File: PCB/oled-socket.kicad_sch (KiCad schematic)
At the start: 16 parts, among them IC17 TPS6734IDR, J5 3-2328724-1

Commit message: change OLED voltage converter to compatible (in-stock) part
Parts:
- IC17: value TPS6734IDR -> TPS6734ID; Arrow Part Number TPS6734IDR -> TPS6734ID; Mouser Part Number 595-TPS6734IDR -> 595-TPS6734ID
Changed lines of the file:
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@@
       (effects (font (size 1.27 1.27)))
     )
-    (property "Value" "TPS6734IDR" (at 207.01 103.0279 0)
+    (property "Value" "TPS6734ID" (at 207.01 103.0279 0)
       (effects (font (size 1.27 1.27)))
     )
@@
       (effects (font (size 1.27 1.27)) (justify left) hide)
     )
-    (property "Mouser Part Number" "595-TPS6734IDR" (at 217.17 119.38 0)
+    (property "Mouser Part Number" "595-TPS6734ID" (at 217.17 119.38 0)
       (effects (font (size 1.27 1.27)) (justify left) hide)
     )
@@
       (effects (font (size 1.27 1.27)) (justify left) hide)
     )
-    (property "Arrow Part Number" "TPS6734IDR" (at 217.17 124.46 0)
+    (property "Arrow Part Number" "TPS6734ID" (at 217.17 124.46 0)
       (effects (font (size 1.27 1.27)) (justify left) hide)
     )
@@
     )
     (property "Note" "RM \"R\" SUFFIX FOR CPT. PART" (at 207.01 118.11 0)
-      (effects (font (size 1.27 1.27)))
+      (effects (font (size 1.27 1.27)) hide)
     )
     (pin "1")

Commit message: add pullup/down resistors and fix oro 6p lines with boot1/0
closes #24
closes #21
closes #15
closes #12
closes #6
closes #3
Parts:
- added R10 (x2): 10k, SamacSys_Parts:RESC5025X65N, symbol SamacSys_Parts:RC2010JK-0710KL
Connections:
- net +3V3: now also R10.1
- net CS: now also R10.2
- net GND: now also R10.1
- net ~{RST}: now also R10.2

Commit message: put pulldowns on unused OLED data lines and add a 510k to pin 13
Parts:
- removed R10: 10k, SamacSys_Parts:RESC5025X65N, symbol SamacSys_Parts:RC2010JK-0710KL
- added R10 (x7): 10k, SamacSys_Parts:RESC5025X65N, symbol SamacSys_Parts:RC2010JK-0710KL
- added R13: 510K, RESC1608X55N, symbol SamacSys_Parts:CR0603-JW-514ELF
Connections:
- net GND: now also R10.2, R10.2, R10.2, R10.2, R10.2, R10.2, R10.2, R13.2; no longer J5.24, J5.25, J5.26, J5.27, J5.28, J5.29
- net ~{RST}: now also R10.1
- net at J5.7: now also R13.1
- new net D2: J5.24, R10.1
- new net D3: J5.25, R10.1
- new net D4: J5.26, R10.1
- new net D5: J5.27, R10.1
- new net D6: J5.28, R10.1
- new net D7: J5.29, R10.1
- no-connect marks 6 -> 5
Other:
- note added: "10K"
- moved on the sheet: C20, C21, R10

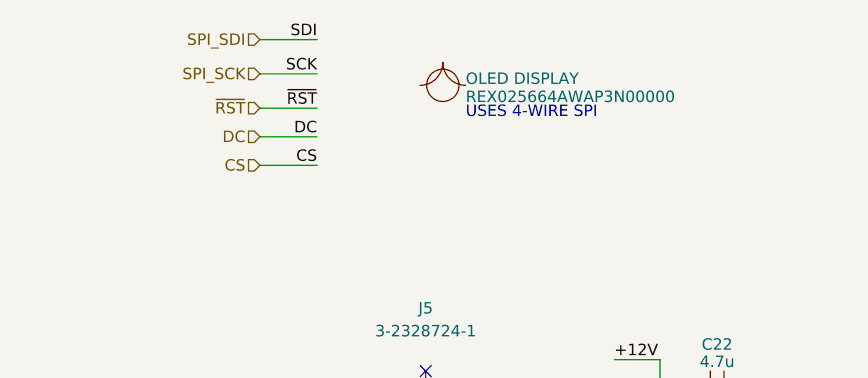
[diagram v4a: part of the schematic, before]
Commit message: add debug pins to signal lines (closes #16)
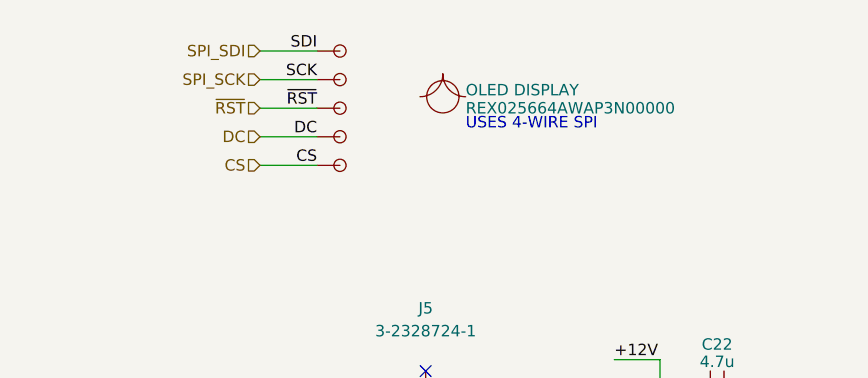
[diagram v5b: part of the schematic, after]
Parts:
- added DBG5 (x5): ~, Oro Footprints:DebugPin, symbol Oro:DebugPin
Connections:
- net CS: now also DBG5.1
- net DC: now also DBG5.1
- net SPI_SCK: now also DBG5.1
- net SPI_SDI: now also DBG5.1
- net ~{RST}: now also DBG5.1
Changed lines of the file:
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@@
     (stroke (width 0) (type default))
   )
-  (wire (pts (xy 67.945 40.64) (xy 74.295 40.64))
+  (wire (pts (xy 67.945 41.91) (xy 74.295 41.91))
     (stroke (width 0) (type default))
   )
@@
     (stroke (width 0) (type default))
   )
-  (wire (pts (xy 67.945 44.45) (xy 74.295 44.45))
+  (wire (pts (xy 67.945 45.085) (xy 74.295 45.085))
     (stroke (width 0) (type default))
   )
@@
     (effects (font (size 1.27 1.27)) (justify left bottom))
   )
-  (text "USES 4-WIRE SPI" (at 90.805 49.53 0)
+  (text "USES 4-WIRE SPI" (at 90.805 50.8 0)
     (effects (font (size 1.27 1.27)) (justify left bottom))
   )
@@
     (effects (font (size 1.27 1.27)) (justify right bottom))
   )
-  (label "SDI" (at 74.295 40.64 180) (fields_autoplaced)
+  (label "SDI" (at 74.295 41.91 180) (fields_autoplaced)
     (effects (font (size 1.27 1.27)) (justify right bottom))
   )
@@
     (effects (font (size 1.27 1.27)) (justify right bottom))
   )
-  (label "SCK" (at 74.295 44.45 180) (fields_autoplaced)
+  (label "SCK" (at 74.295 45.085 180) (fields_autoplaced)
     (effects (font (size 1.27 1.27)) (justify right bottom))
   )
@@
     (effects (font (size 1.27 1.27)) (justify right))
   )
-  (hierarchical_label "SPI_SDI" (shape input) (at 67.945 40.64 180) (fields_autoplaced)
+  (hierarchical_label "SPI_SDI" (shape input) (at 67.945 41.91 180) (fields_autoplaced)
     (effects (font (size 1.27 1.27)) (justify right))
   )
-  (hierarchical_label "SPI_SCK" (shape input) (at 67.945 44.45 180) (fields_autoplaced)
+  (hierarchical_label "SPI_SCK" (shape input) (at 67.945 45.085 180) (fields_autoplaced)
     (effects (font (size 1.27 1.27)) (justify right))
   )
@@
     )
   )
-  (symbol (lib_id "Oro:BOM Part") (at 88.265 45.72 0) (unit 1)
+  (symbol (lib_id "Oro:BOM Part") (at 88.265 46.99 0) (unit 1)
     (in_bom yes) (on_board no) (dnp no)
-    (property "Reference" "B2" (at 90.17 45.0763 0)
-      (effects (font (size 1.27 1.27)) (justify left) hide)
-    )
-    (property "Value" "REX025664AWAP3N00000" (at 90.805 46.99 0)
+    (property "Reference" "B2" (at 90.17 46.3463 0)
+      (effects (font (size 1.27 1.27)) (justify left) hide)
+    )
+    (property "Value" "REX025664AWAP3N00000" (at 90.805 48.26 0)
       (effects (font (size 1.27 1.27)) (justify left))
     )
-    (property "Footprint" "" (at 88.265 45.72 0)
-      (effects (font (size 1.27 1.27)) hide)
-    )
-    (property "Datasheet" "https://www.mouser.de/datasheet/2/271/REX025664AWAP3N00000_V_E_20191218-1888866.pdf" (at 88.265 45.72 0)
-      (effects (font (size 1.27 1.27)) hide)
-    )
-    (property "Sim.Enable" "0" (at 88.265 45.72 0)
-      (effects (font (size 1.27 1.27)) hide)
-    )
-    (property "Manufacturer_Part_Number" "REX025664AWAP3N00000" (at 88.265 45.72 0)
-      (effects (font (size 1.27 1.27)) hide)
-    )
-    (property "Mouser Part Number" "668-REX025664AWAP3N" (at 88.265 45.72 0)
-      (effects (font (size 1.27 1.27)) hide)
-    )
-    (property "Note" "OLED DISPLAY" (at 90.805 45.72 0)
+    (property "Footprint" "" (at 88.265 46.99 0)
+      (effects (font (size 1.27 1.27)) hide)
+    )
+    (property "Datasheet" "https://www.mouser.de/datasheet/2/271/REX025664AWAP3N00000_V_E_20191218-1888866.pdf" (at 88.265 46.99 0)
+      (effects (font (size 1.27 1.27)) hide)
+    )
+    (property "Sim.Enable" "0" (at 88.265 46.99 0)
+      (effects (font (size 1.27 1.27)) hide)
+    )
+    (property "Manufacturer_Part_Number" "REX025664AWAP3N00000" (at 88.265 46.99 0)
+      (effects (font (size 1.27 1.27)) hide)
+    )
+    (property "Mouser Part Number" "668-REX025664AWAP3N" (at 88.265 46.99 0)
+      (effects (font (size 1.27 1.27)) hide)
+    )
+    (property "Note" "OLED DISPLAY" (at 90.805 46.99 0)
       (effects (font (size 1.27 1.27)) (justify left bottom))
     )
@@
     )
   )
+  (symbol (lib_id "Oro:DebugPin") (at 74.295 45.085 0) (unit 1)
+    (in_bom no) (on_board yes) (dnp no)
+    (property "Reference" "DBG5" (at 80.01 45.085 0)
+      (effects (font (size 1.27 1.27)) hide)
+    )
+    (property "Value" "~" (at 74.295 45.085 0)
+      (effects (font (size 1.27 1.27)) hide)
+    )
+    (property "Footprint" "Oro Footprints:DebugPin" (at 75.565 42.545 0)
+      (effects (font (size 1.27 1.27)) hide)
+    )
+    (property "Datasheet" "" (at 74.295 45.085 0)
+      (effects (font (size 1.27 1.27)) hide)
+    )
+    (property "Sim.Enable" "0" (at 88.265 42.545 0)
+      (effects (font (size 1.27 1.27)) hide)
+    )
+    (pin "1")
+    (instances
+      (project "OroLink"
+        (path "/e89dcd22-1250-4a5b-b778-1c95a0dd623d/f955395e-bf1a-4ef3-9cfe-ec9d49f66988"
+          (reference "DBG5") (unit 1)
+        )
+        (path "/e89dcd22-1250-4a5b-b778-1c95a0dd623d/1b3eede1-74b0-4c0b-b4f1-7ec1bfc1f54f"
+          (reference "DBG13") (unit 1)
+        )
+      )
+    )
+  )
   (symbol (lib_id "SamacSys_Parts:CR0603-JW-514ELF") (at 50.165 97.79 270) (unit 1)
     (in_bom yes) (on_board yes) (dnp no) (fields_autoplaced)
@@
     )
   )
+  (symbol (lib_id "Oro:DebugPin") (at 74.295 41.91 0) (unit 1)
+    (in_bom no) (on_board yes) (dnp no)
+    (property "Reference" "DBG5" (at 80.01 41.91 0)
+      (effects (font (size 1.27 1.27)) hide)
+    )
+    (property "Value" "~" (at 74.295 41.91 0)
+      (effects (font (size 1.27 1.27)) hide)
+    )
+    (property "Footprint" "Oro Footprints:DebugPin" (at 75.565 39.37 0)
+      (effects (font (size 1.27 1.27)) hide)
+    )
+    (property "Datasheet" "" (at 74.295 41.91 0)
+      (effects (font (size 1.27 1.27)) hide)
+    )
+    (property "Sim.Enable" "0" (at 88.265 39.37 0)
+      (effects (font (size 1.27 1.27)) hide)
+    )
+    (pin "1")
+    (instances
+      (project "OroLink"
+        (path "/e89dcd22-1250-4a5b-b778-1c95a0dd623d/f955395e-bf1a-4ef3-9cfe-ec9d49f66988"
+          (reference "DBG5") (unit 1)
+        )
+        (path "/e89dcd22-1250-4a5b-b778-1c95a0dd623d/1b3eede1-74b0-4c0b-b4f1-7ec1bfc1f54f"
+          (reference "DBG12") (unit 1)
+        )
+      )
+    )
+  )
   (symbol (lib_id "SamacSys_Parts:RC2010JK-0710KL") (at 56.515 156.845 270) (unit 1)
     (in_bom yes) (on_board yes) (dnp no)
@@
     )
   )
+  (symbol (lib_id "Oro:DebugPin") (at 74.295 48.26 0) (unit 1)
+    (in_bom no) (on_board yes) (dnp no)
+    (property "Reference" "DBG5" (at 80.01 48.26 0)
+      (effects (font (size 1.27 1.27)) hide)
+    )
+    (property "Value" "~" (at 74.295 48.26 0)
+      (effects (font (size 1.27 1.27)) hide)
+    )
+    (property "Footprint" "Oro Footprints:DebugPin" (at 75.565 45.72 0)
+      (effects (font (size 1.27 1.27)) hide)
+    )
+    (property "Datasheet" "" (at 74.295 48.26 0)
+      (effects (font (size 1.27 1.27)) hide)
+    )
+    (property "Sim.Enable" "0" (at 88.265 45.72 0)
+      (effects (font (size 1.27 1.27)) hide)
+    )
+    (pin "1")
+    (instances
+      (project "OroLink"
+        (path "/e89dcd22-1250-4a5b-b778-1c95a0dd623d/f955395e-bf1a-4ef3-9cfe-ec9d49f66988"
+          (reference "DBG5") (unit 1)
+        )
+        (path "/e89dcd22-1250-4a5b-b778-1c95a0dd623d/1b3eede1-74b0-4c0b-b4f1-7ec1bfc1f54f"
+          (reference "DBG14") (unit 1)
+        )
+      )
+    )
+  )
+  (symbol (lib_id "Oro:DebugPin") (at 74.295 54.61 0) (unit 1)
+    (in_bom no) (on_board yes) (dnp no)
+    (property "Reference" "DBG5" (at 80.01 54.61 0)
+      (effects (font (size 1.27 1.27)) hide)
+    )
+    (property "Value" "~" (at 74.295 54.61 0)
+      (effects (font (size 1.27 1.27)) hide)
+    )
+    (property "Footprint" "Oro Footprints:DebugPin" (at 75.565 52.07 0)
+      (effects (font (size 1.27 1.27)) hide)
+    )
+    (property "Datasheet" "" (at 74.295 54.61 0)
+      (effects (font (size 1.27 1.27)) hide)
+    )
+    (property "Sim.Enable" "0" (at 88.265 52.07 0)
+      (effects (font (size 1.27 1.27)) hide)
+    )
+    (pin "1")
+    (instances
+      (project "OroLink"
+        (path "/e89dcd22-1250-4a5b-b778-1c95a0dd623d/f955395e-bf1a-4ef3-9cfe-ec9d49f66988"
+          (reference "DBG5") (unit 1)
+        )
+        (path "/e89dcd22-1250-4a5b-b778-1c95a0dd623d/1b3eede1-74b0-4c0b-b4f1-7ec1bfc1f54f"
+          (reference "DBG16") (unit 1)
+        )
+      )
+    )
+  )
   (symbol (lib_id "power:GND") (at 40.005 127.635 0) (unit 1)
     (in_bom yes) (on_board yes) (dnp no)
@@
         )
       )
+    )
+  )
+  (symbol (lib_id "Oro:DebugPin") (at 74.295 51.435 0) (unit 1)
+    (in_bom no) (on_board yes) (dnp no)
+    (property "Reference" "DBG5" (at 80.01 51.435 0)
+      (effects (font (size 1.27 1.27)) hide)
+    )
+    (property "Value" "~" (at 74.295 51.435 0)
+      (effects (font (size 1.27 1.27)) hide)
+    )
+    (property "Footprint" "Oro Footprints:DebugPin" (at 75.565 48.895 0)
+      (effects (font (size 1.27 1.27)) hide)
+    )
+    (property "Datasheet" "" (at 74.295 51.435 0)
+      (effects (font (size 1.27 1.27)) hide)
+    )
+    (property "Sim.Enable" "0" (at 88.265 48.895 0)
+      (effects (font (size 1.27 1.27)) hide)
+    )
+    (pin "1")
+    (instances
+      (project "OroLink"
+        (path "/e89dcd22-1250-4a5b-b778-1c95a0dd623d/f955395e-bf1a-4ef3-9cfe-ec9d49f66988"
+          (reference "DBG5") (unit 1)
+        )
+        (path "/e89dcd22-1250-4a5b-b778-1c95a0dd623d/1b3eede1-74b0-4c0b-b4f1-7ec1bfc1f54f"
+          (reference "DBG15") (unit 1)
+        )
+      )

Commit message: switch 10k and 4.7k resistors to smaller packages (closes #32)
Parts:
- R10: footprint SamacSys_Parts:RESC5025X65N -> RESC5025X65N
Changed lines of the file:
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@@
       (effects (font (size 1.27 1.27)) (justify left) hide)
     )
-    (property "Footprint" "SamacSys_Parts:RESC5025X65N" (at 80.01 170.815 0)
+    (property "Footprint" "RESC5025X65N" (at 80.01 170.815 0)
       (effects (font (size 1.27 1.27)) (justify left) hide)
     )
@@
       (effects (font (size 1.27 1.27)) (justify left) hide)
     )
-    (property "Footprint" "SamacSys_Parts:RESC5025X65N" (at 71.12 170.815 0)
+    (property "Footprint" "RESC5025X65N" (at 71.12 170.815 0)
       (effects (font (size 1.27 1.27)) (justify left) hide)
     )
@@
         )
         (path "/e89dcd22-1250-4a5b-b778-1c95a0dd623d/1b3eede1-74b0-4c0b-b4f1-7ec1bfc1f54f"
-          (reference "DBG13") (unit 1)
+          (reference "DBG8") (unit 1)
         )
       )
@@
       (effects (font (size 1.27 1.27)) (justify left) hide)
     )
-    (property "Footprint" "SamacSys_Parts:RESC5025X65N" (at 62.23 170.815 0)
+    (property "Footprint" "RESC5025X65N" (at 62.23 170.815 0)
       (effects (font (size 1.27 1.27)) (justify left) hide)
     )
@@
         )
         (path "/e89dcd22-1250-4a5b-b778-1c95a0dd623d/1b3eede1-74b0-4c0b-b4f1-7ec1bfc1f54f"
-          (reference "DBG12") (unit 1)
+          (reference "DBG7") (unit 1)
         )
       )
@@
       (effects (font (size 1.27 1.27)) (justify left) hide)
     )
-    (property "Footprint" "SamacSys_Parts:RESC5025X65N" (at 57.785 170.815 0)
+    (property "Footprint" "RESC5025X65N" (at 57.785 170.815 0)
       (effects (font (size 1.27 1.27)) (justify left) hide)
     )
@@
       (effects (font (size 1.27 1.27)))
     )
-    (property "Footprint" "SamacSys_Parts:RESC5025X65N" (at 104.14 167.64 0)
+    (property "Footprint" "RESC5025X65N" (at 104.14 167.64 0)
       (effects (font (size 1.27 1.27)) (justify left) hide)
     )
@@
       (effects (font (size 1.27 1.27)) (justify left) hide)
     )
-    (property "Footprint" "SamacSys_Parts:RESC5025X65N" (at 66.675 170.815 0)
+    (property "Footprint" "RESC5025X65N" (at 66.675 170.815 0)
       (effects (font (size 1.27 1.27)) (justify left) hide)
     )
@@
         )
         (path "/e89dcd22-1250-4a5b-b778-1c95a0dd623d/1b3eede1-74b0-4c0b-b4f1-7ec1bfc1f54f"
-          (reference "DBG14") (unit 1)
+          (reference "DBG9") (unit 1)
         )
       )
@@
         )
         (path "/e89dcd22-1250-4a5b-b778-1c95a0dd623d/1b3eede1-74b0-4c0b-b4f1-7ec1bfc1f54f"
-          (reference "DBG16") (unit 1)
+          (reference "DBG11") (unit 1)
         )
       )
@@
       (effects (font (size 1.27 1.27)) (justify left) hide)
     )
-    (property "Footprint" "SamacSys_Parts:RESC5025X65N" (at 75.565 170.815 0)
+    (property "Footprint" "RESC5025X65N" (at 75.565 170.815 0)
       (effects (font (size 1.27 1.27)) (justify left) hide)
     )
@@
         )
         (path "/e89dcd22-1250-4a5b-b778-1c95a0dd623d/1b3eede1-74b0-4c0b-b4f1-7ec1bfc1f54f"
-          (reference "DBG15") (unit 1)
+          (reference "DBG10") (unit 1)
         )
       )
@@
       (effects (font (size 1.27 1.27)) (justify left) hide)
     )
-    (property "Footprint" "SamacSys_Parts:RESC5025X65N" (at 53.34 170.815 0)
+    (property "Footprint" "RESC5025X65N" (at 53.34 170.815 0)
       (effects (font (size 1.27 1.27)) (justify left) hide)
     )
@@
       (effects (font (size 1.27 1.27)) (justify right))
     )
-    (property "Footprint" "SamacSys_Parts:RESC5025X65N" (at 190.5 92.71 0)
-      (effects (font (size 1.27 1.27)) (justify left) hide)
-    )
+    (property "Footprint" "RESC5025X65N" (at 190.5 92.71 0)
+      (effects (font (size 1.27 1.27)) (justify left) hide)
+    )

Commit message: actually reduce 10k package size (ref #32)
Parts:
- R10: footprint RESC5025X65N -> RESC1005X40N; symbol SamacSys_Parts:RC2010JK-0710KL -> SamacSys_Parts:RK73H1ETTP1002F; Arrow Part Number RC2010JK-0710KL -> RK73H1ETTP1002F; Arrow Price/Stock https://www.arrow.com/en/products/rc2010jk-0710kl/yageo -> https://www.arrow.com/en/products/rk73h1ettp1002f/koa-speer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; Height 0.65 -> 0.4; Manufacturer_Name KEMET -> KOA Speer; Manufacturer_Part_Number RC2010JK-0710KL -> RK73H1ETTP1002F; Mouser Part Number 603-RC2010JK-0710KL -> 660-RK73H1ETTP1002F; Mouser Price/Stock https://www.mouser.co.uk/ProductDetail/YAGEO/RC2010JK-0710K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 -> https://www.mouser.co.uk/ProductDetail/KOA-Speer/RK73H1ETTP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
